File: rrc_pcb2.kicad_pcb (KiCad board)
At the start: 2 copper layers, 138.4 x 68.2 mm, 14 parts, among them J1 battery_header, J2 buzzer_toggle_pin, U2 Teensy4.1, U3 BN220-GPS, U5 MS5611, U6 logo, U7 Conn_01x02_Male-Connector

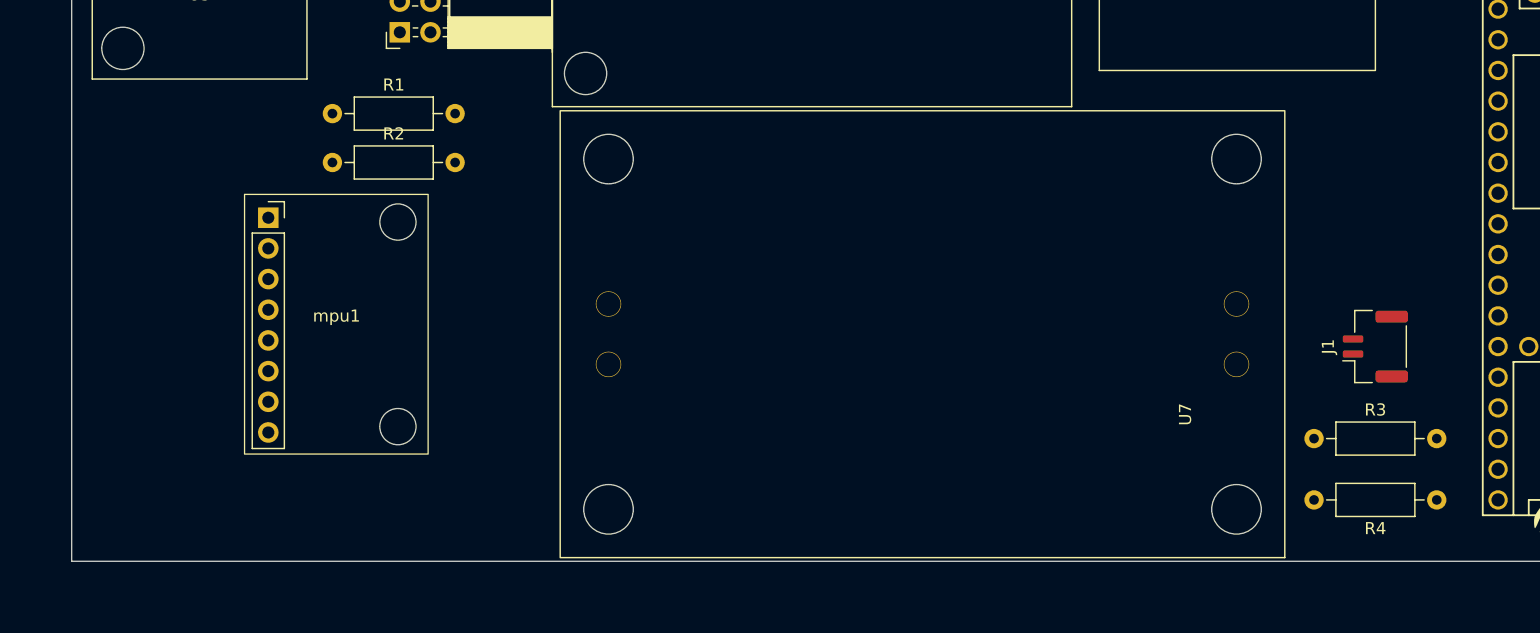
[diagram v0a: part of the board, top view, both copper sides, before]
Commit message: added 4 pin led
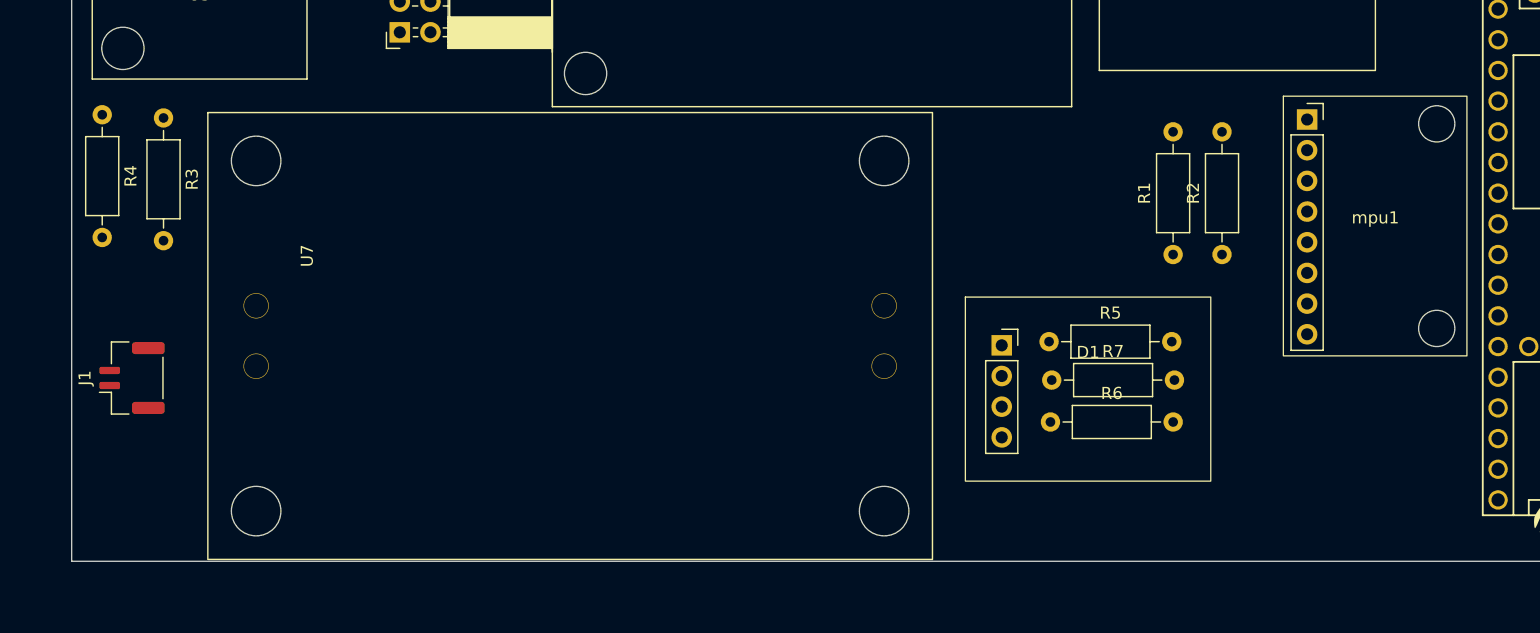
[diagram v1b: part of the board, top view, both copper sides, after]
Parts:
- added D1: ASMB-MTB0-0A3A2, LED_4pin:LED_4PIN, F.Cu at (126.1, 72.1)
- added R5: R-Device, Resistor_THT:R_Axial_DIN0207_L6.3mm_D2.5mm_P10.16mm_Horizontal, F.Cu at (122.8, 70.7)
- added R6: R-Device, Resistor_THT:R_Axial_DIN0207_L6.3mm_D2.5mm_P10.16mm_Horizontal, F.Cu at (123.0, 77.4)
- added R7: R-Device, Resistor_THT:R_Axial_DIN0207_L6.3mm_D2.5mm_P10.16mm_Horizontal, F.Cu at (123.1, 73.9)
- U7: value Conn_01x02_Male-Connector -> voltReg
- moved R4 115.0 mm to (44.4, 51.9), turned to -90 degrees
- moved J1 103.0 mm to (46.9, 73.7)
- moved R3 98.9 mm to (49.5, 52.2), turned to -90 degrees
- moved U7 96.5 mm to (53.2, 51.7), turned to 0 degrees
- moved mpu1 86.4 mm to (149.9, 61.0)
- moved R2 74.1 mm to (137.2, 63.5), turned to 90 degrees
- moved R1 70.6 mm to (133.1, 63.5), turned to 90 degrees
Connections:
- U2 pad 30: FSYNC -> unconnected-(U2-38_CS1_IN1-Pad30)
- U2 pad 32: INT1 -> B
- U2 pad 33: unconnected-(U2-41_A17-Pad33) -> G
- U2 pad 35: unconnected-(U2-13_SCK_LED-Pad35) -> R

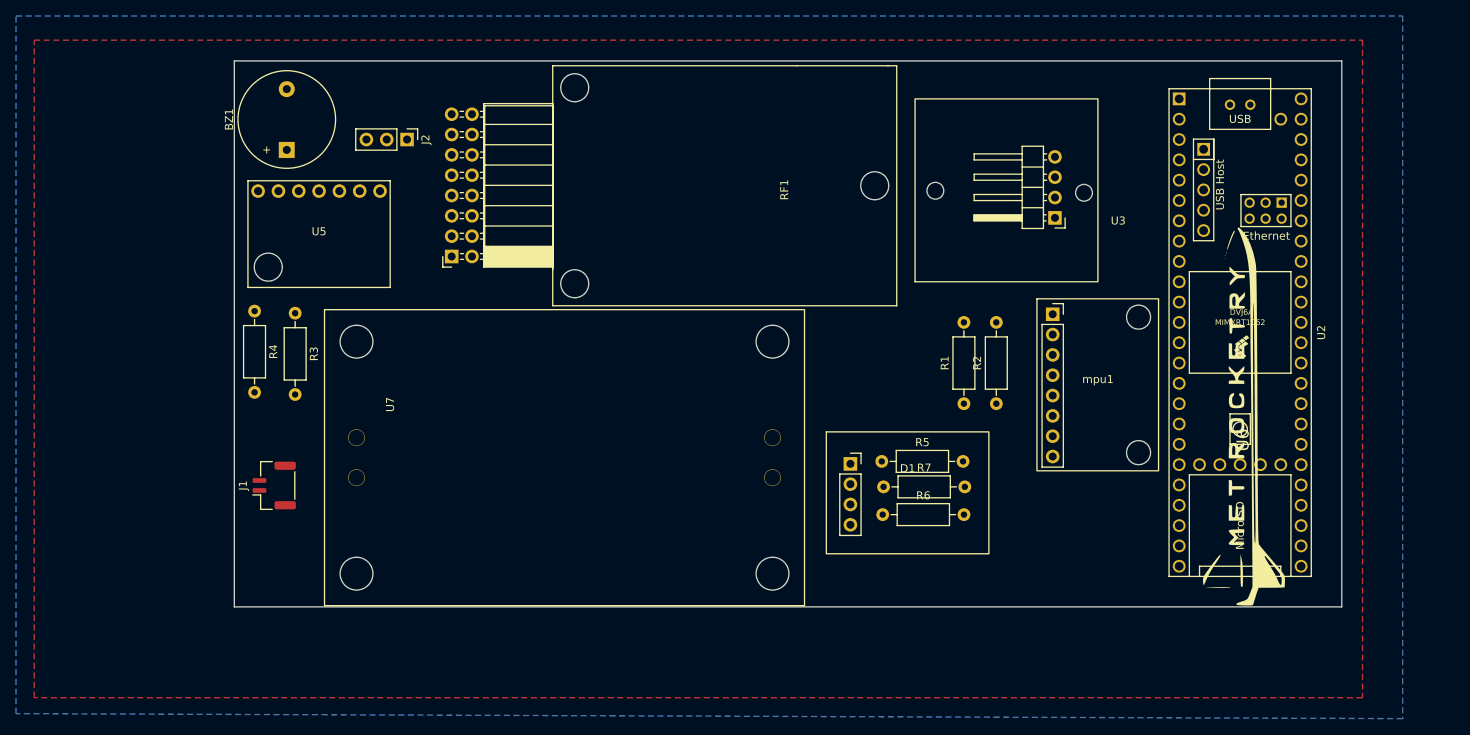
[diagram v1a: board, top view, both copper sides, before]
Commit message: updated pcb ina160 and traces
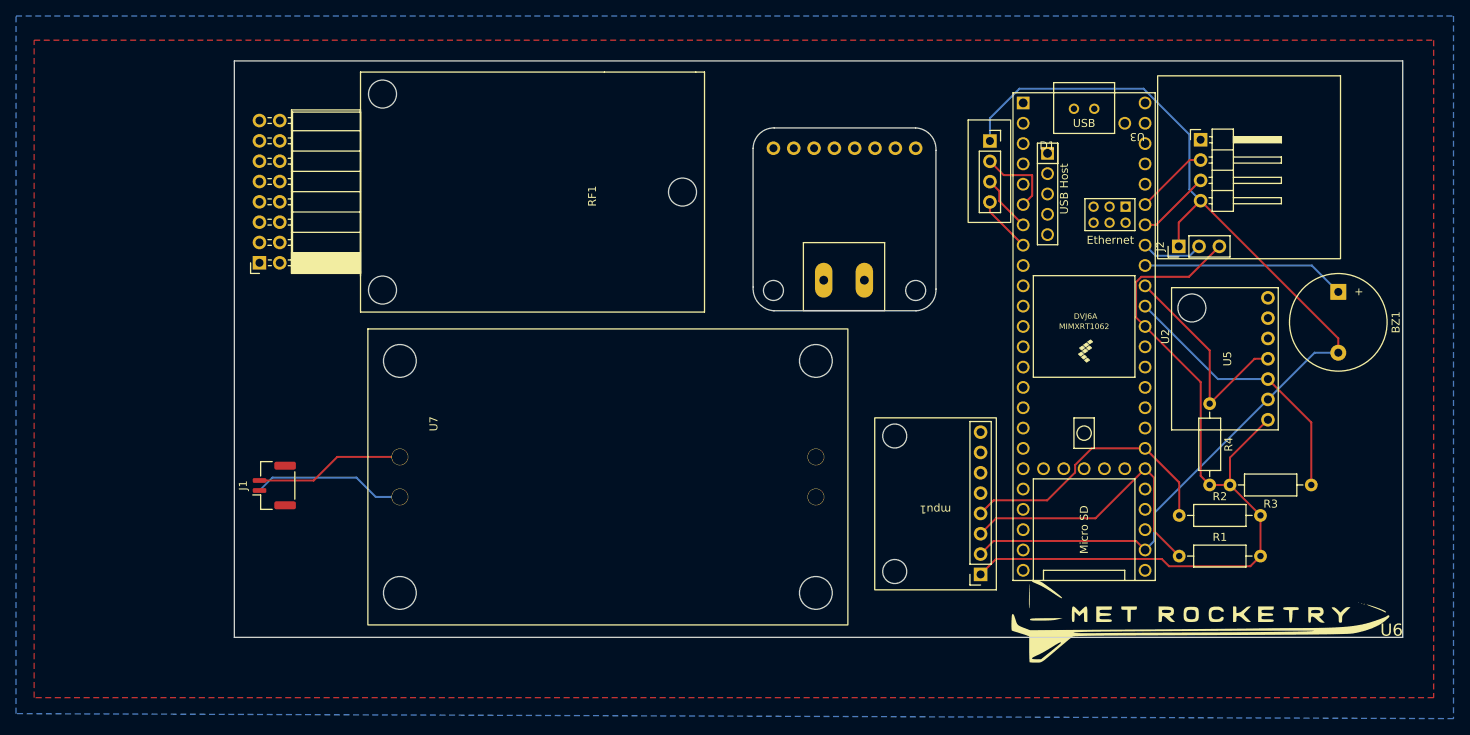
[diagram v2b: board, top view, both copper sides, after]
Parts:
- removed R5, R6, R7: R-Device, Resistor_THT:R_Axial_DIN0207_L6.3mm_D2.5mm_P10.16mm_Horizontal
- added U4: INA260, INA260:INA260, F.Cu at (118.1, 40.2)
- U7: value voltReg -> Conn_01x02_Male-Connector
- moved BZ1 132.6 mm to (179.9, 49.5), turned to -90 degrees
- moved R3 128.8 mm to (176.5, 73.7), turned to 180 degrees
- moved U5 124.9 mm to (174.9, 57.9), turned to 90 degrees
- moved R4 120.0 mm to (163.8, 63.5)
- moved J2 97.4 mm to (160.0, 43.8), turned to 90 degrees
- moved U3 56.8 mm to (180.2, 45.4), turned to 180 degrees
- moved D1 44.0 mm to (143.5, 31.8)
- moved R1 33.0 mm to (160.0, 82.5), turned to 0 degrees
- moved R2 26.8 mm to (160.0, 77.5), turned to 0 degrees
- moved mpu1 25.4 mm to (129.5, 76.2), turned to 180 degrees
- moved RF1 24.0 mm to (57.7, 22.0)
- moved U6 24.0 mm to (159.7, 90.6), turned to 0 degrees
- moved U2 19.5 mm to (148.1, 55.1)
- moved U7 5.93 mm to (58.6, 54.2)
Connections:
- D1 pad 2: Net-(D1-BK) -> B
- D1 pad 3: Net-(D1-GK) -> G
- D1 pad 4: Net-(D1-RK) -> R
- R1 pad 1: SCL -> SCL1
- R2 pad 1: SDA -> SDA1
- R3 pad 1: SCL1 -> SCL2
- R4 pad 1: SDA1 -> SDA2
- U2 pad 16: unconnected-(U2-24_A10_TX6_SCL2-Pad16) -> SCL2
- U2 pad 17: SDA1 -> SDA2
- U2 pad 32: B -> unconnected-(U2-40_A16-Pad32)
- U2 pad 33: G -> unconnected-(U2-41_A17-Pad33)
- U2 pad 35: R -> unconnected-(U2-13_SCK_LED-Pad35)
- U2 pad 4: unconnected-(U2-2_OUT2-Pad4) -> B
- U2 pad 5: unconnected-(U2-3_LRCLK2-Pad5) -> G
- U2 pad 6: unconnected-(U2-4_BCLK2-Pad6) -> R
- U5 pad 3: SCL1 -> SCL2
- U5 pad 4: SDA1 -> SDA2
- mpu1 pad 3: SCL -> SCL1
- mpu1 pad 4: SDA -> SDA1
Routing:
- net T_GND: track 0.00 -> 131.6 mm
- net T_VCC: track 0.00 -> 101.2 mm
- net SCL1: track 0.00 -> 36.6 mm
- net SDA1: track 0.00 -> 34.6 mm
- net SCL2: track 0.00 -> 34.6 mm
- net SDA2: track 0.00 -> 27.7 mm
- net Net-(BZ1--): track 0.00 -> 25.5 mm
- net Net-(J1-Pin_1): track 0.00 -> 19.2 mm
- net Net-(J1-Pin_2): track 0.00 -> 18.8 mm
- net B: track 0.00 -> 10.1 mm
- net TX7: track 0.00 -> 9.24 mm
- net RX7: track 0.00 -> 9.24 mm
- net Net-(J2-Pin_2): track 0.00 -> 7.78 mm
- net G: track 0.00 -> 7.12 mm
- net R: track 0.00 -> 7.12 mm
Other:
- board size 138.4 x 68.2 mm -> 146.1 x 72.1 mm

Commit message: PCB2
Added INA to footprint, connected everything up, & generated gerber files.
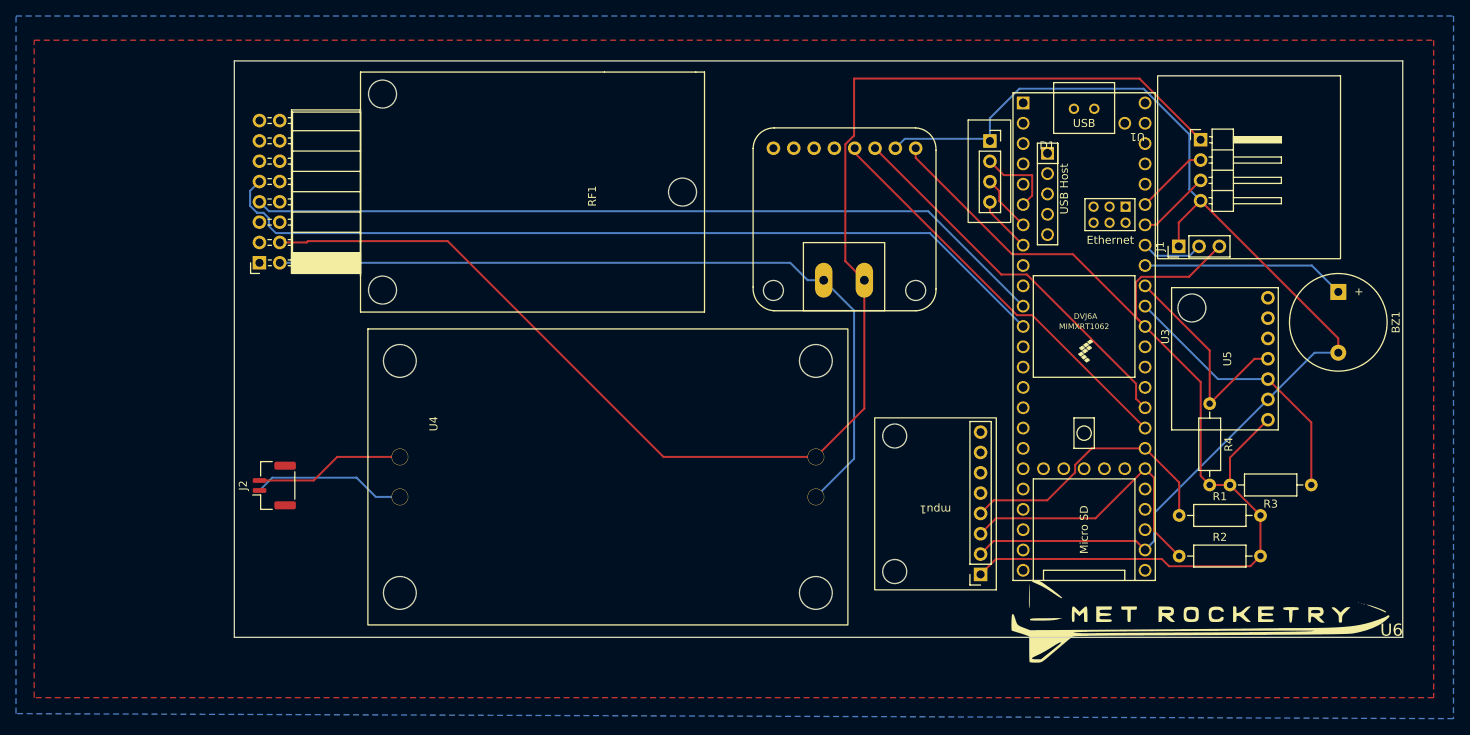
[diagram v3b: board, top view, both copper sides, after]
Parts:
- U4: renamed from U7; value Conn_01x02_Male-Connector -> voltReg
- renumbered J2 to J1, J1 to J2, R2 to R1, R1 to R2, U3 to U1, U4 to U2, U2 to U3
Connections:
- RF1 pad +5V: (no net) -> VCC
- RF1 pad GND: (no net) -> GND
- RF1 pad SIRX: (no net) -> RX2
- RF1 pad SITX: (no net) -> TX2
- U2 pad 1: unconnected-(U4-VIN+-Pad1) -> VCC
- U2 pad 10: GND -> unconnected-(U2-IN--Pad10)
- U2 pad 2: unconnected-(U4-VIN--Pad2) -> GND
- U2 pad 9: VCC -> unconnected-(U2-IN+-Pad9)
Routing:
- net VCC: track 0.00 -> 176.0 mm
- net TX2: track 0.00 -> 107.0 mm
- net RX2: track 0.00 -> 100.9 mm
- net GND: track 0.00 -> 99.5 mm
- net SDA: track 0.00 -> 51.1 mm
- net SCL: track 0.00 -> 48.3 mm
- net T_VCC: track 101.2 -> 139.9 mm
- net T_GND: track 131.6 -> 144.0 mm
